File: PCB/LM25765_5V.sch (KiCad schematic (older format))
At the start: 8 parts, among them U5 LM2576S-3.3

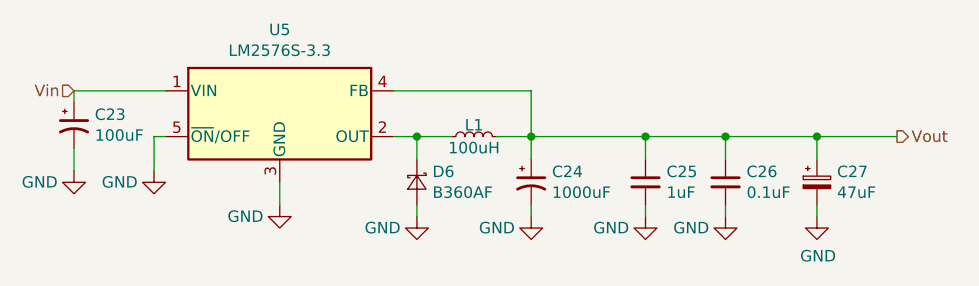
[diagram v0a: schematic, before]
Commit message: Replaced 3v3 regulator with 5v
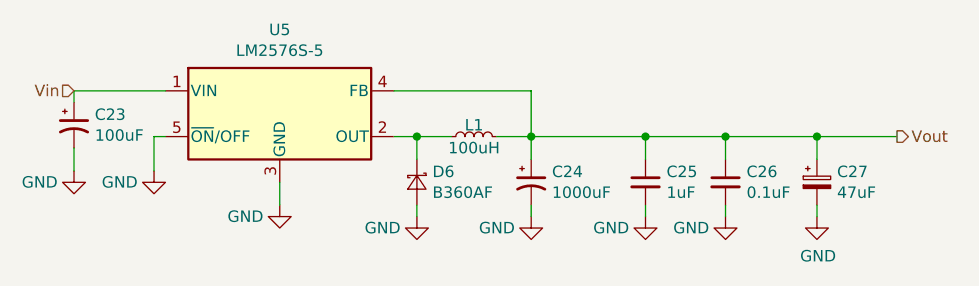
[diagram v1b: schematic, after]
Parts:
- U5: value LM2576S-3.3 -> LM2576S-5
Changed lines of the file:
@@
 $Descr A4 11693 8268
 encoding utf-8
-Sheet 11 25
+Sheet 12 25
 Title ""
 Date ""
@@
 AR Path="/5E880E11/5E9C913B/5B713F8D" Ref="U5"  Part="1"
 F 0 "U5" H 5200 4117 50  0000 C CNN
-F 1 "LM2576S-3.3" H 5200 4026 50  0000 C CNN
+F 1 "LM2576S-5" H 5200 4026 50  0000 C CNN
 F 2 "Package_TO_SOT_SMD:TO-263-5_TabPin3" H 5200 3500 50  0001 L CIN
 F 3 "http://www.ti.com/lit/ds/symlink/lm2576.pdf" H 5200 3750 50  0001 C CNN

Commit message: Added Humidity and temperature sensors
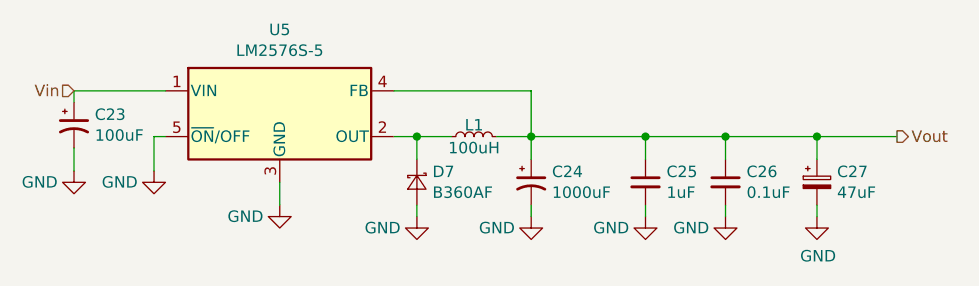
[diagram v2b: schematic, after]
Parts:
- renumbered D6 to D7
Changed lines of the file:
@@
 AR Path="/5E880E11/5E904307/5B713F64" Ref="#PWR?"  Part="1"
 AR Path="/5E880E11/5E9C764B/5B713F64" Ref="#PWR?"  Part="1"
-AR Path="/5E880E11/5E9C913B/5B713F64" Ref="#PWR074"  Part="1"
-F 0 "#PWR074" H 5200 3900 50  0001 C CNN
+AR Path="/5E880E11/5E9C913B/5B713F64" Ref="#PWR077"  Part="1"
+F 0 "#PWR077" H 5200 3900 50  0001 C CNN
 F 1 "GND" H 5050 4100 50  0000 C CNN
 F 2 "" H 5200 4150 50  0001 C CNN
@@
 AR Path="/5E880E11/5E904307/5B713FAA" Ref="#PWR?"  Part="1"
 AR Path="/5E880E11/5E9C764B/5B713FAA" Ref="#PWR?"  Part="1"
-AR Path="/5E880E11/5E9C913B/5B713FAA" Ref="#PWR076"  Part="1"
-F 0 "#PWR076" H 6300 3950 50  0001 C CNN
+AR Path="/5E880E11/5E9C913B/5B713FAA" Ref="#PWR079"  Part="1"
+F 0 "#PWR079" H 6300 3950 50  0001 C CNN
 F 1 "GND" H 6150 4150 50  0000 C CNN
 F 2 "" H 6300 4200 50  0001 C CNN
@@
 AR Path="/5E880E11/5E904307/5B713FBB" Ref="#PWR?"  Part="1"
 AR Path="/5E880E11/5E9C764B/5B713FBB" Ref="#PWR?"  Part="1"
-AR Path="/5E880E11/5E9C913B/5B713FBB" Ref="#PWR075"  Part="1"
-F 0 "#PWR075" H 5800 3950 50  0001 C CNN
+AR Path="/5E880E11/5E9C913B/5B713FBB" Ref="#PWR078"  Part="1"
+F 0 "#PWR078" H 5800 3950 50  0001 C CNN
 F 1 "GND" H 5650 4150 50  0000 C CNN
 F 2 "" H 5800 4200 50  0001 C CNN
@@
 AR Path="/5E880E11/5E904307/5B713FDF" Ref="D?"  Part="1"
 AR Path="/5E880E11/5E9C764B/5B713FDF" Ref="D?"  Part="1"
-AR Path="/5E880E11/5E9C913B/5B713FDF" Ref="D6"  Part="1"
-F 0 "D6" V 5754 4118 50  0000 L CNN
+AR Path="/5E880E11/5E9C913B/5B713FDF" Ref="D7"  Part="1"
+F 0 "D7" V 5754 4118 50  0000 L CNN
 F 1 "B360AF" V 5845 4118 50  0000 L CNN
 F 2 "Diode_SMD:D_SMA" V 5800 4050 50  0001 C CNN
@@
 AR Path="/5E880E11/5E904307/5E8CA26E" Ref="#PWR?"  Part="1"
 AR Path="/5E880E11/5E9C764B/5E8CA26E" Ref="#PWR?"  Part="1"
-AR Path="/5E880E11/5E9C913B/5E8CA26E" Ref="#PWR079"  Part="1"
-F 0 "#PWR079" H 7550 3950 50  0001 C CNN
+AR Path="/5E880E11/5E9C913B/5E8CA26E" Ref="#PWR082"  Part="1"
+F 0 "#PWR082" H 7550 3950 50  0001 C CNN
 F 1 "GND" H 7555 4027 50  0000 C CNN
 F 2 "" H 7550 4200 50  0001 C CNN
@@
 AR Path="/5E880E11/5E904307/5E8CA270" Ref="#PWR?"  Part="1"
 AR Path="/5E880E11/5E9C764B/5E8CA270" Ref="#PWR?"  Part="1"
-AR Path="/5E880E11/5E9C913B/5E8CA270" Ref="#PWR077"  Part="1"
-F 0 "#PWR077" H 6800 3950 50  0001 C CNN
+AR Path="/5E880E11/5E9C913B/5E8CA270" Ref="#PWR080"  Part="1"
+F 0 "#PWR080" H 6800 3950 50  0001 C CNN
 F 1 "GND" H 6650 4150 50  0000 C CNN
 F 2 "" H 6800 4200 50  0001 C CNN
@@
 AR Path="/5E880E11/5E904307/5E8CA271" Ref="#PWR?"  Part="1"
 AR Path="/5E880E11/5E9C764B/5E8CA271" Ref="#PWR?"  Part="1"
-AR Path="/5E880E11/5E9C913B/5E8CA271" Ref="#PWR078"  Part="1"
-F 0 "#PWR078" H 7150 3950 50  0001 C CNN
+AR Path="/5E880E11/5E9C913B/5E8CA271" Ref="#PWR081"  Part="1"
+F 0 "#PWR081" H 7150 3950 50  0001 C CNN
 F 1 "GND" H 7000 4150 50  0000 C CNN
 F 2 "" H 7150 4200 50  0001 C CNN
@@
 AR Path="/5E880E11/5E904307/5E8CA268" Ref="#PWR?"  Part="1"
 AR Path="/5E880E11/5E9C764B/5E8CA268" Ref="#PWR?"  Part="1"
-AR Path="/5E880E11/5E9C913B/5E8CA268" Ref="#PWR073"  Part="1"
-F 0 "#PWR073" H 4650 3750 50  0001 C CNN
+AR Path="/5E880E11/5E9C913B/5E8CA268" Ref="#PWR076"  Part="1"
+F 0 "#PWR076" H 4650 3750 50  0001 C CNN
 F 1 "GND" H 4500 3950 50  0000 C CNN
 F 2 "" H 4650 4000 50  0001 C CNN
@@
 AR Path="/5E880E11/5E904307/5E8CA26A" Ref="#PWR?"  Part="1"
 AR Path="/5E880E11/5E9C764B/5E8CA26A" Ref="#PWR?"  Part="1"
-AR Path="/5E880E11/5E9C913B/5E8CA26A" Ref="#PWR072"  Part="1"
-F 0 "#PWR072" H 4300 3750 50  0001 C CNN
+AR Path="/5E880E11/5E9C913B/5E8CA26A" Ref="#PWR075"  Part="1"
+F 0 "#PWR075" H 4300 3750 50  0001 C CNN
 F 1 "GND" H 4150 3950 50  0000 C CNN
 F 2 "" H 4300 4000 50  0001 C CNN

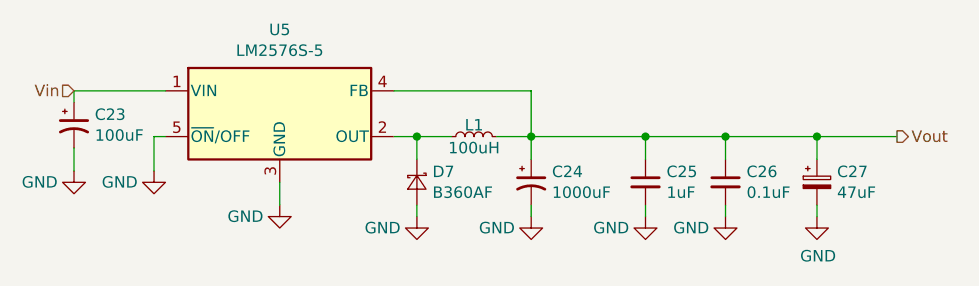
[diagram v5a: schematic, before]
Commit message: Added remaining test points
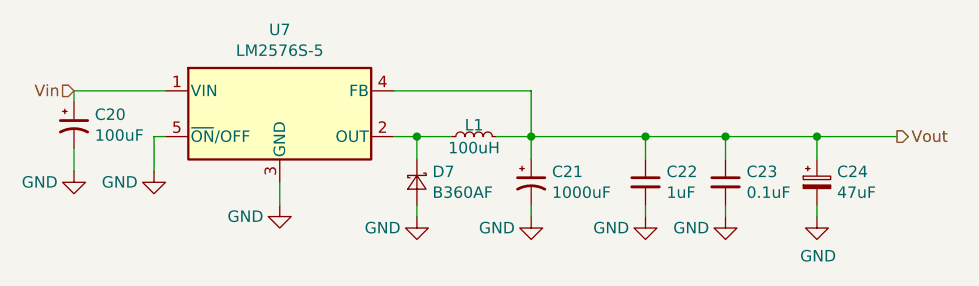
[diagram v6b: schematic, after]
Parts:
- renumbered C23 to C20, C24 to C21, C25 to C22, C26 to C23, C27 to C24, U5 to U7
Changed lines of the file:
@@
 AR Path="/5E880E11/5E904307/5B713F64" Ref="#PWR?"  Part="1"
 AR Path="/5E880E11/5E9C764B/5B713F64" Ref="#PWR?"  Part="1"
-AR Path="/5E880E11/5E9C913B/5B713F64" Ref="#PWR077"  Part="1"
-F 0 "#PWR077" H 5200 3900 50  0001 C CNN
+AR Path="/5E880E11/5E9C913B/5B713F64" Ref="#PWR073"  Part="1"
+F 0 "#PWR073" H 5200 3900 50  0001 C CNN
 F 1 "GND" H 5050 4100 50  0000 C CNN
 F 2 "" H 5200 4150 50  0001 C CNN
@@
 AR Path="/5E880E11/5E904307/5B713F8D" Ref="U?"  Part="1"
 AR Path="/5E880E11/5E9C764B/5B713F8D" Ref="U?"  Part="1"
-AR Path="/5E880E11/5E9C913B/5B713F8D" Ref="U5"  Part="1"
-F 0 "U5" H 5200 4117 50  0000 C CNN
+AR Path="/5E880E11/5E9C913B/5B713F8D" Ref="U7"  Part="1"
+F 0 "U7" H 5200 4117 50  0000 C CNN
 F 1 "LM2576S-5" H 5200 4026 50  0000 C CNN
 F 2 "Package_TO_SOT_SMD:TO-263-5_TabPin3" H 5200 3500 50  0001 L CIN
@@
 AR Path="/5E880E11/5E904307/5B713FA0" Ref="C?"  Part="1"
 AR Path="/5E880E11/5E9C764B/5B713FA0" Ref="C?"  Part="1"
-AR Path="/5E880E11/5E9C913B/5B713FA0" Ref="C24"  Part="1"
-F 0 "C24" H 6391 4096 50  0000 L CNN
+AR Path="/5E880E11/5E9C913B/5B713FA0" Ref="C21"  Part="1"
+F 0 "C21" H 6391 4096 50  0000 L CNN
 F 1 "1000uF" H 6391 4005 50  0000 L CNN
 F 2 "Capacitor_SMD:CP_Elec_8x10" H 6300 4050 50  0001 C CNN
@@
 AR Path="/5E880E11/5E904307/5B713FAA" Ref="#PWR?"  Part="1"
 AR Path="/5E880E11/5E9C764B/5B713FAA" Ref="#PWR?"  Part="1"
-AR Path="/5E880E11/5E9C913B/5B713FAA" Ref="#PWR079"  Part="1"
-F 0 "#PWR079" H 6300 3950 50  0001 C CNN
+AR Path="/5E880E11/5E9C913B/5B713FAA" Ref="#PWR075"  Part="1"
+F 0 "#PWR075" H 6300 3950 50  0001 C CNN
 F 1 "GND" H 6150 4150 50  0000 C CNN
 F 2 "" H 6300 4200 50  0001 C CNN
@@
 AR Path="/5E880E11/5E904307/5B713FBB" Ref="#PWR?"  Part="1"
 AR Path="/5E880E11/5E9C764B/5B713FBB" Ref="#PWR?"  Part="1"
-AR Path="/5E880E11/5E9C913B/5B713FBB" Ref="#PWR078"  Part="1"
-F 0 "#PWR078" H 5800 3950 50  0001 C CNN
+AR Path="/5E880E11/5E9C913B/5B713FBB" Ref="#PWR074"  Part="1"
+F 0 "#PWR074" H 5800 3950 50  0001 C CNN
 F 1 "GND" H 5650 4150 50  0000 C CNN
 F 2 "" H 5800 4200 50  0001 C CNN
@@
 AR Path="/5E880E11/5E904307/5B9CEDF5" Ref="C?"  Part="1"
 AR Path="/5E880E11/5E9C764B/5B9CEDF5" Ref="C?"  Part="1"
-AR Path="/5E880E11/5E9C913B/5B9CEDF5" Ref="C25"  Part="1"
-F 0 "C25" H 6892 4096 50  0000 L CNN
+AR Path="/5E880E11/5E9C913B/5B9CEDF5" Ref="C22"  Part="1"
+F 0 "C22" H 6892 4096 50  0000 L CNN
 F 1 "1uF" H 6892 4005 50  0000 L CNN
 F 2 "Capacitors:0603" H 6800 4050 50  0001 C CNN
@@
 AR Path="/5E880E11/5E904307/5B9CEDFC" Ref="C?"  Part="1"
 AR Path="/5E880E11/5E9C764B/5B9CEDFC" Ref="C?"  Part="1"
-AR Path="/5E880E11/5E9C913B/5B9CEDFC" Ref="C26"  Part="1"
-F 0 "C26" H 7242 4096 50  0000 L CNN
+AR Path="/5E880E11/5E9C913B/5B9CEDFC" Ref="C23"  Part="1"
+F 0 "C23" H 7242 4096 50  0000 L CNN
 F 1 "0.1uF" H 7242 4005 50  0000 L CNN
 F 2 "Capacitors:0603" H 7150 4050 50  0001 C CNN
@@
 AR Path="/5E880E11/5E904307/5E8CA26E" Ref="#PWR?"  Part="1"
 AR Path="/5E880E11/5E9C764B/5E8CA26E" Ref="#PWR?"  Part="1"
-AR Path="/5E880E11/5E9C913B/5E8CA26E" Ref="#PWR082"  Part="1"
-F 0 "#PWR082" H 7550 3950 50  0001 C CNN
+AR Path="/5E880E11/5E9C913B/5E8CA26E" Ref="#PWR078"  Part="1"
+F 0 "#PWR078" H 7550 3950 50  0001 C CNN
 F 1 "GND" H 7555 4027 50  0000 C CNN
 F 2 "" H 7550 4200 50  0001 C CNN
@@
 AR Path="/5E880E11/5E904307/5E8CA26F" Ref="C?"  Part="1"
 AR Path="/5E880E11/5E9C764B/5E8CA26F" Ref="C?"  Part="1"
-AR Path="/5E880E11/5E9C913B/5E8CA26F" Ref="C27"  Part="1"
-F 0 "C27" H 7638 4096 50  0000 L CNN
+AR Path="/5E880E11/5E9C913B/5E8CA26F" Ref="C24"  Part="1"
+F 0 "C24" H 7638 4096 50  0000 L CNN
 F 1 "47uF" H 7638 4005 50  0000 L CNN
 F 2 "Capacitor_SMD:CP_Elec_4x5.4" H 7550 4050 50  0001 C CNN
@@
 AR Path="/5E880E11/5E904307/5E8CA270" Ref="#PWR?"  Part="1"
 AR Path="/5E880E11/5E9C764B/5E8CA270" Ref="#PWR?"  Part="1"
-AR Path="/5E880E11/5E9C913B/5E8CA270" Ref="#PWR080"  Part="1"
-F 0 "#PWR080" H 6800 3950 50  0001 C CNN
+AR Path="/5E880E11/5E9C913B/5E8CA270" Ref="#PWR076"  Part="1"
+F 0 "#PWR076" H 6800 3950 50  0001 C CNN
 F 1 "GND" H 6650 4150 50  0000 C CNN
 F 2 "" H 6800 4200 50  0001 C CNN
@@
 AR Path="/5E880E11/5E904307/5E8CA271" Ref="#PWR?"  Part="1"
 AR Path="/5E880E11/5E9C764B/5E8CA271" Ref="#PWR?"  Part="1"
-AR Path="/5E880E11/5E9C913B/5E8CA271" Ref="#PWR081"  Part="1"
-F 0 "#PWR081" H 7150 3950 50  0001 C CNN
+AR Path="/5E880E11/5E9C913B/5E8CA271" Ref="#PWR077"  Part="1"
+F 0 "#PWR077" H 7150 3950 50  0001 C CNN
 F 1 "GND" H 7000 4150 50  0000 C CNN
 F 2 "" H 7150 4200 50  0001 C CNN
@@
 AR Path="/5E880E11/5E904307/5E8CA268" Ref="#PWR?"  Part="1"
 AR Path="/5E880E11/5E9C764B/5E8CA268" Ref="#PWR?"  Part="1"
-AR Path="/5E880E11/5E9C913B/5E8CA268" Ref="#PWR076"  Part="1"
-F 0 "#PWR076" H 4650 3750 50  0001 C CNN
+AR Path="/5E880E11/5E9C913B/5E8CA268" Ref="#PWR072"  Part="1"
+F 0 "#PWR072" H 4650 3750 50  0001 C CNN
 F 1 "GND" H 4500 3950 50  0000 C CNN
 F 2 "" H 4650 4000 50  0001 C CNN
@@
 AR Path="/5E880E11/5E904307/5E8CA26A" Ref="#PWR?"  Part="1"
 AR Path="/5E880E11/5E9C764B/5E8CA26A" Ref="#PWR?"  Part="1"
-AR Path="/5E880E11/5E9C913B/5E8CA26A" Ref="#PWR075"  Part="1"
-F 0 "#PWR075" H 4300 3750 50  0001 C CNN
+AR Path="/5E880E11/5E9C913B/5E8CA26A" Ref="#PWR071"  Part="1"
+F 0 "#PWR071" H 4300 3750 50  0001 C CNN
 F 1 "GND" H 4150 3950 50  0000 C CNN
 F 2 "" H 4300 4000 50  0001 C CNN
@@
 AR Path="/5E880E11/5E904307/5E8CA269" Ref="C?"  Part="1"
 AR Path="/5E880E11/5E9C764B/5E8CA269" Ref="C?"  Part="1"
-AR Path="/5E880E11/5E9C913B/5E8CA269" Ref="C23"  Part="1"
-F 0 "C23" H 4391 3846 50  0000 L CNN
+AR Path="/5E880E11/5E9C913B/5E8CA269" Ref="C20"  Part="1"
+F 0 "C20" H 4391 3846 50  0000 L CNN
 F 1 "100uF" H 4391 3755 50  0000 L CNN
 F 2 "Capacitor_SMD:CP_Elec_5x5.4" H 4300 3800 50  0001 C CNN

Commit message: Added majority footprints
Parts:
- C22, C23: footprint Capacitors:0603 -> Capacitor_SMD:C_0603_1608Metric
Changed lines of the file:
@@
 F 0 "C22" H 6892 4096 50  0000 L CNN
 F 1 "1uF" H 6892 4005 50  0000 L CNN
-F 2 "Capacitors:0603" H 6800 4050 50  0001 C CNN
+F 2 "Capacitor_SMD:C_0603_1608Metric" H 6800 4050 50  0001 C CNN
 F 3 "" H 6800 4050 50  0001 C CNN
 F 4 "Power Supply" H 6800 4050 50  0001 C CNN "Functional Block"
@@
 F 0 "C23" H 7242 4096 50  0000 L CNN
 F 1 "0.1uF" H 7242 4005 50  0000 L CNN
-F 2 "Capacitors:0603" H 7150 4050 50  0001 C CNN
+F 2 "Capacitor_SMD:C_0603_1608Metric" H 7150 4050 50  0001 C CNN
 F 3 "" H 7150 4050 50  0001 C CNN
 F 4 "Power Supply" H 7150 4050 50  0001 C CNN "Functional Block"

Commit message: Added correct Alu cap MPNs
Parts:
- C20: MPN EEE-1AA101SP -> EEE-FT1C101AR
- C21: MPN UWT0J102MNL1GS -> EEE-0JA102UP; Manufacturer (none) -> Panasonic
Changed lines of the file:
@@
 F 2 "Capacitor_SMD:CP_Elec_8x10" H 6300 4050 50  0001 C CNN
 F 3 "" H 6300 4050 50  0001 C CNN
-F 4 "UWT0J102MNL1GS" H 6300 4050 50  0001 C CNN "MPN"
+F 4 "EEE-0JA102UP" H 6300 4050 50  0001 C CNN "MPN"
 F 5 "Power Supply" H 6300 4050 50  0001 C CNN "Functional Block"
 F 6 "Aluminium Film" H -700 -100 50  0001 C CNN "Dielectric"
@@
 F 8 "General Purpose" H -700 -100 50  0001 C CNN "Impedance"
 F 9 "1000hr @ 85degC" H -700 -100 50  0001 C CNN "Lifetime @ Temperature"
+F 10 "Panasonic" H 6300 4050 50  0001 C CNN "Manufacturer"
 	1    6300 4050
 	1    0    0    -1
@@
 F 2 "Capacitor_SMD:CP_Elec_5x5.4" H 4300 3800 50  0001 C CNN
 F 3 "" H 4300 3800 50  0001 C CNN
-F 4 "EEE-1AA101SP" H 0   0   50  0001 C CNN "MPN"
+F 4 "EEE-FT1C101AR" H 0   0   50  0001 C CNN "MPN"
 F 5 "Panasonic" H 0   0   50  0001 C CNN "Manufacturer"
 F 6 "Power Supply" H 4300 3800 50  0001 C CNN "Functional Block"
